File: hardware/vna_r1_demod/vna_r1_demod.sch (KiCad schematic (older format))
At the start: 13 parts

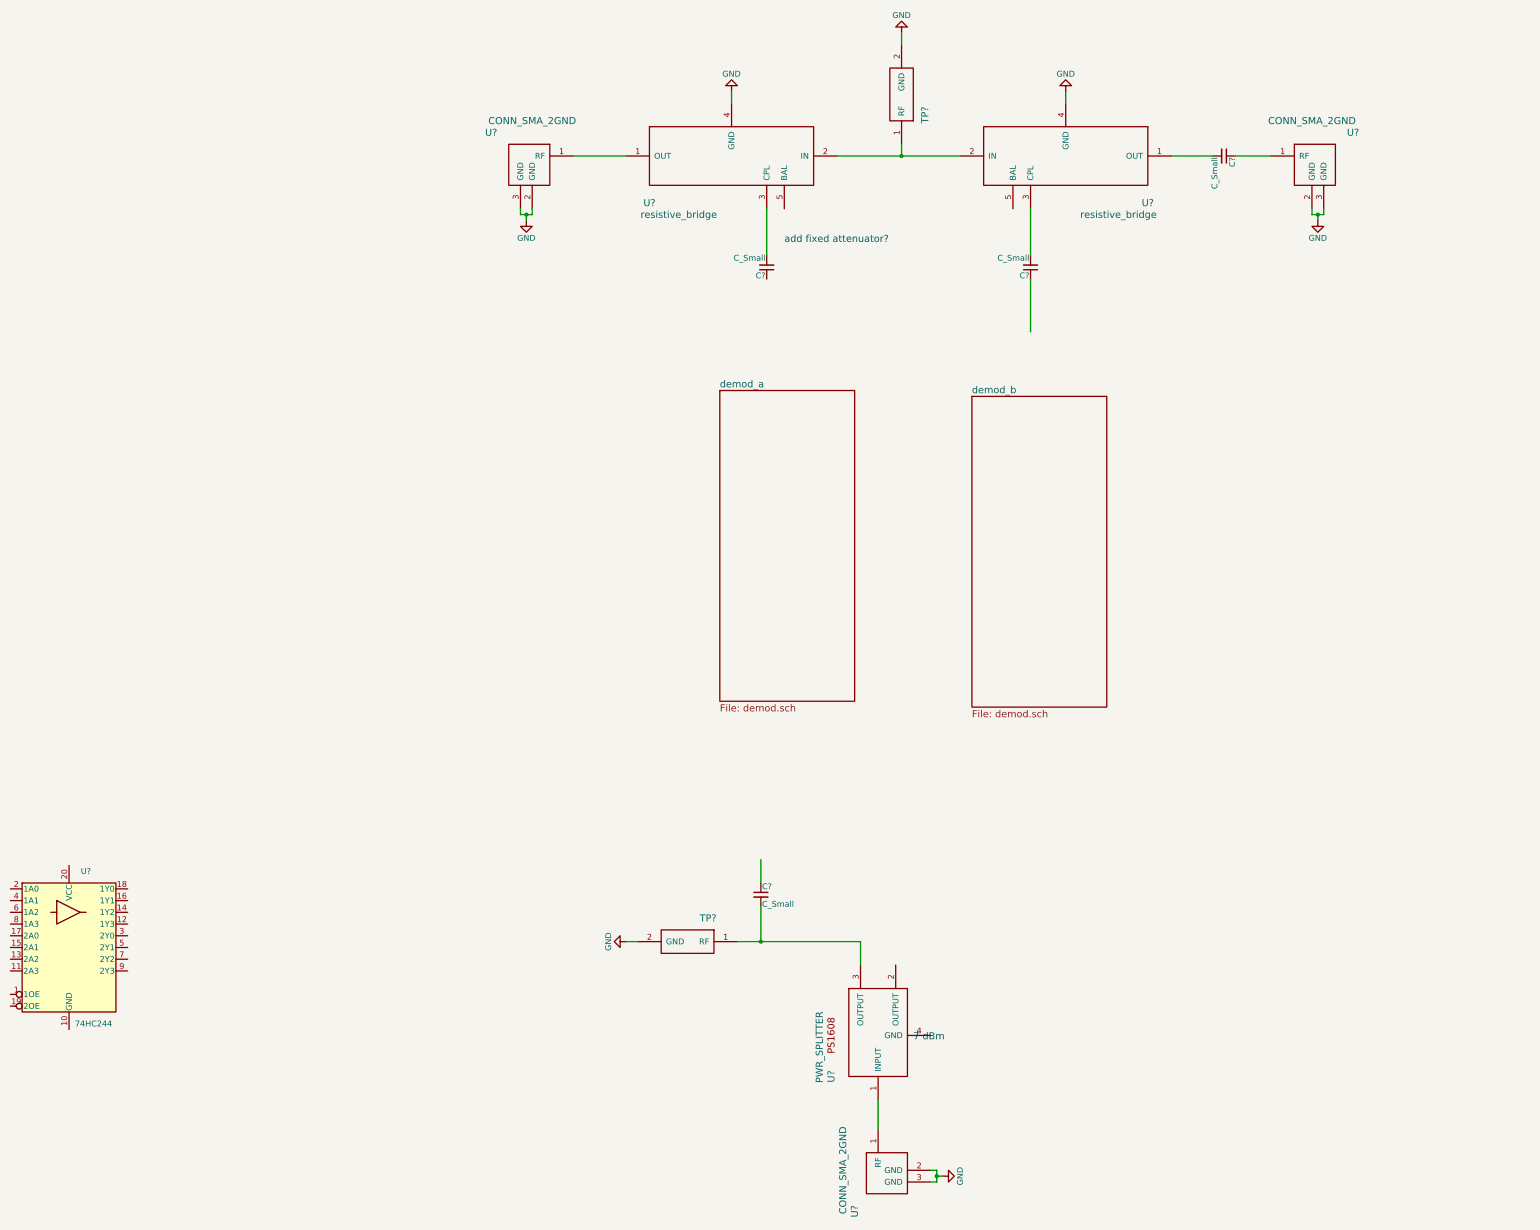
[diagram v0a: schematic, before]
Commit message: work on vna r1 demod schematic
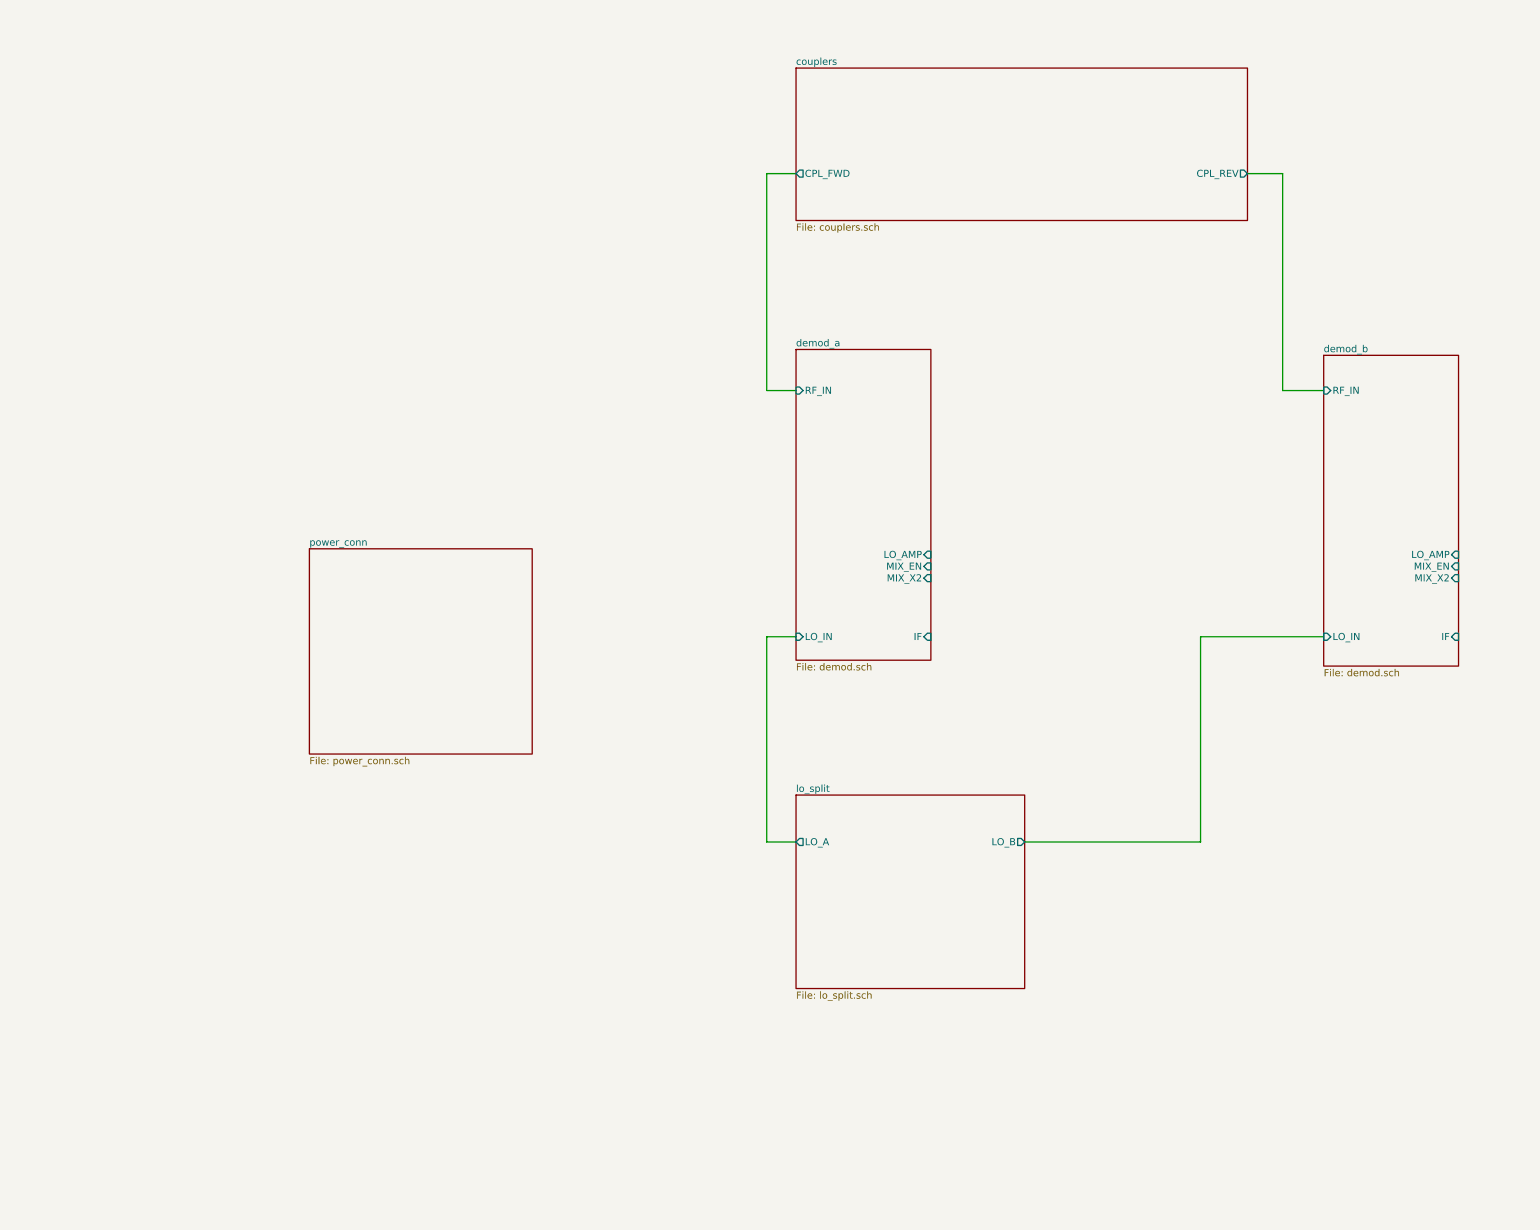
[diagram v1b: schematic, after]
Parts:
- removed C? (x4): C_Small, symbol C_Small
- removed TP? (x2): TP_RF, symbol TP_RF
- removed U? (x2): resistive_bridge, symbol resistive_bridge
- removed U? (x3): CONN_SMA_2GND, symbol CONN_SMA_2GND
- removed U?: PWR_SPLITTER, symbol PWR_SPLITTER
- removed U?: 74HC244, symbol 74HC244
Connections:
- net labels removed: GND
- wire segments 29 -> 12
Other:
- note removed: "7 dBm"
- note removed: "add fixed attenuator?"

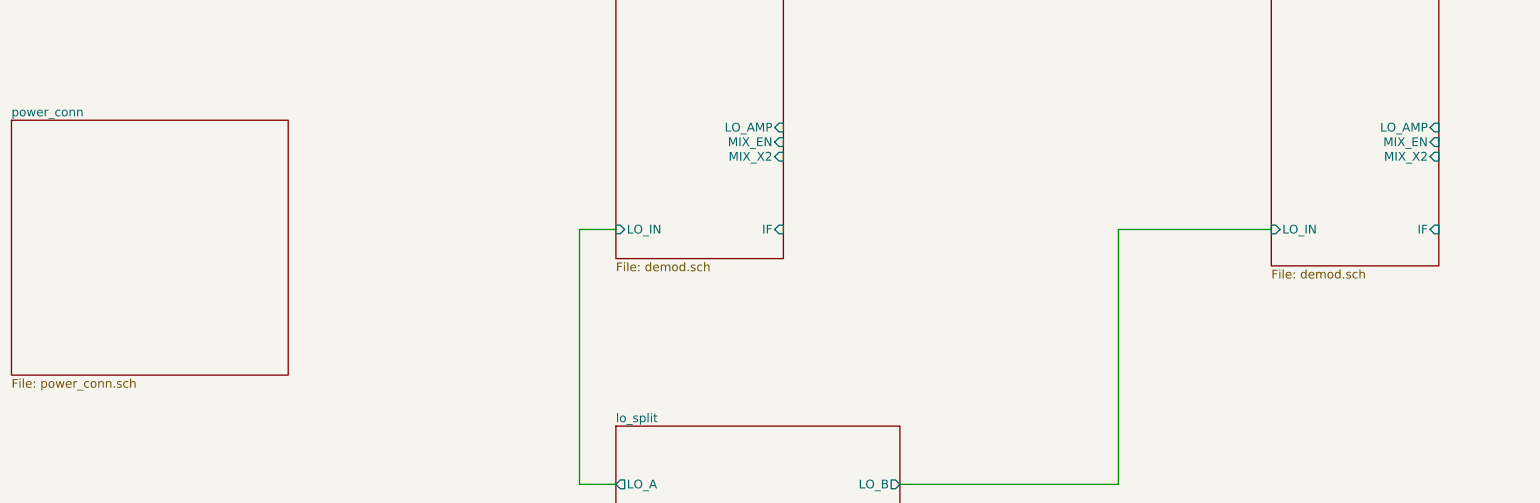
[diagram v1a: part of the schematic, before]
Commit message: ethernet and usb layout on vna control board..
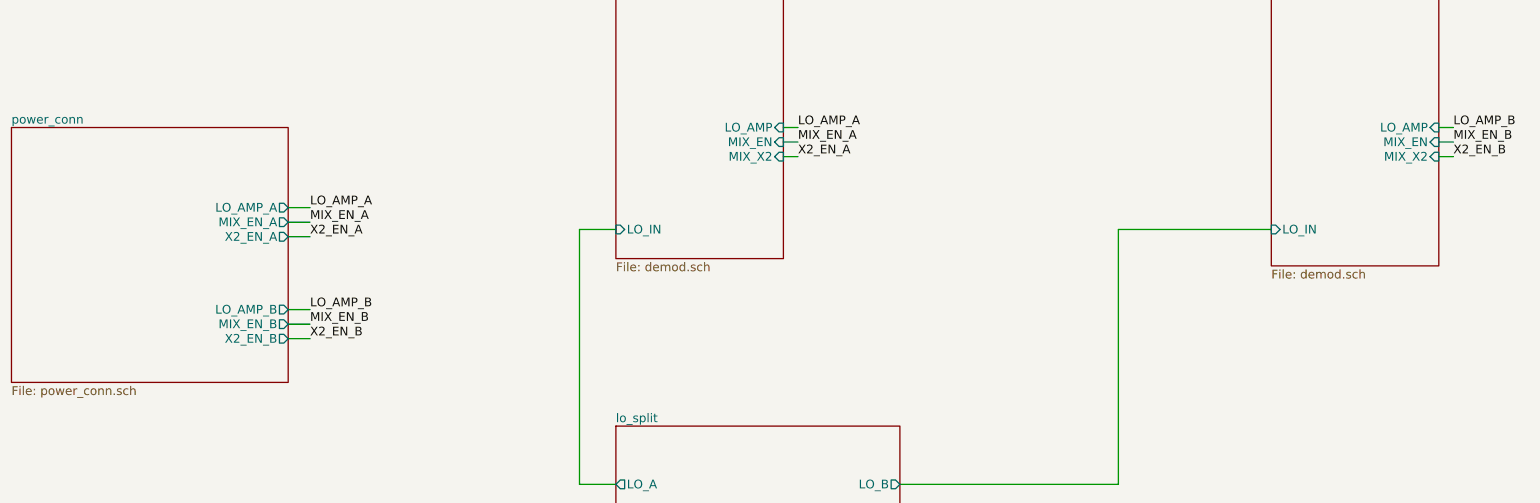
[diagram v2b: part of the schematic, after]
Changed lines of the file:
@@
 F4 "MIX_EN" I R 10100 5500 60
 F5 "MIX_X2" I R 10100 5600 60
-F6 "IF" I R 10100 6100 60
-F7 "LO_AMP" I R 10100 5400 60
+F6 "LO_AMP" I R 10100 5400 60
 $EndSheet
 $Sheet
@@
 F4 "MIX_EN" I R 14600 5500 60
 F5 "MIX_X2" I R 14600 5600 60
-F6 "IF" I R 14600 6100 60
-F7 "LO_AMP" I R 14600 5400 60
+F6 "LO_AMP" I R 14600 5400 60
 $EndSheet
 $Sheet
-S 4800 5350 1900 1750
+S 4800 5400 1900 1750
 U 5AC731FA
 F0 "power_conn" 60
 F1 "power_conn.sch" 60
+F2 "LO_AMP_A" O R 6700 5950 60
+F3 "LO_AMP_B" O R 6700 6650 60
+F4 "MIX_EN_A" O R 6700 6050 60
+F5 "X2_EN_A" O R 6700 6150 60
+F6 "MIX_EN_B" O R 6700 6750 60
+F7 "X2_EN_B" O R 6700 6850 60
 $EndSheet
 $Sheet
@@
 Wire Wire Line
 	8700 4000 8950 4000
+Wire Wire Line
+	6700 5950 6850 5950
+Wire Wire Line
+	6700 6050 6850 6050
+Wire Wire Line
+	6700 6150 6850 6150
+Wire Wire Line
+	6700 6650 6850 6650
+Wire Wire Line
+	6700 6750 6850 6750
+Wire Wire Line
+	6700 6850 6850 6850
+Text Label 6850 5950 0    60   ~ 0
+LO_AMP_A
+Text Label 6850 6050 0    60   ~ 0
+MIX_EN_A
+Text Label 6850 6150 0    60   ~ 0
+X2_EN_A
+Text Label 6850 6650 0    60   ~ 0
+LO_AMP_B
+Text Label 6850 6750 0    60   ~ 0
+MIX_EN_B
+Text Label 6850 6850 0    60   ~ 0
+X2_EN_B
+Text Label 14700 5400 0    60   ~ 0
+LO_AMP_B
+Text Label 14700 5500 0    60   ~ 0
+MIX_EN_B
+Text Label 14700 5600 0    60   ~ 0
+X2_EN_B
+Text Label 10200 5400 0    60   ~ 0
+LO_AMP_A
+Text Label 10200 5500 0    60   ~ 0
+MIX_EN_A
+Text Label 10200 5600 0    60   ~ 0
+X2_EN_A
+Wire Wire Line
+	10100 5400 10200 5400
+Wire Wire Line
+	10100 5500 10200 5500
+Wire Wire Line
+	10100 5600 10200 5600
+Wire Wire Line
+	14600 5400 14700 5400
+Wire Wire Line
+	14600 5500 14700 5500
+Wire Wire Line
+	14600 5600 14700 5600
 $EndSCHEMATC

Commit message: finished vna r1 control board?
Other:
- note added: "200 mA"
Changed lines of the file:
@@
 LIBS:tp_rf
 LIBS:hmc65xlp2e
+LIBS:ld39100
 LIBS:vna_r1_demod-cache
 EELAYER 25 0
@@
 Wire Wire Line
 	14600 5600 14700 5600
+Text Notes 9750 3600 0    60   ~ 0
+200 mA
+Text Notes 14300 3600 0    60   ~ 0
+200 mA
 $EndSCHEMATC
